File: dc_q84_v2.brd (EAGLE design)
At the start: 60.6 x 58.4 mm, 61 parts, among them IC2 7805TV, IC3 ADM3095EBRZ, IC4 PIC18F47Q84-I_PT, J1 3-1734577-4, U1 REF3440IDBVR, U2 TCAN330GDR

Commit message: up
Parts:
- removed 24VDC_PWR: 24vdc power, con-molex:22-23-2021
- removed C10, C17: 10uf, rcl:C0805
- removed C16, C9: 0.1uf, rcl:C0805
- removed U1: REF3440IDBVR, REF3440IDBVR:SOT95P280X145-6N
- removed VREF_PWR: 5vdc_vref_pwr, con-molex:22-23-2021
- moved EXT_IO 15.5 mm to (14.0, 39.4), turned to 0 degrees
- moved C3 10.9 mm to (11.4, 34.3)
- moved OS1_10MHZ 9.16 mm to (12.7, 27.9)
- moved TP2 6.84 mm to (15.2, 34.3)
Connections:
- net V+: no longer 24VDC_PWR.1
- net VDD: no longer C10.1, C9.1, U1.4
- net VREF: no longer C16.1, C17.1, U1.5, U1.6, VREF_PWR.1
- net VSS: no longer 24VDC_PWR.2, C10.2, C16.2, C17.2, C9.2, U1.1, U1.2, U1.3, VREF_PWR.2
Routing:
- net CLOCKO: track 121.4 -> 43.2 mm, vias 4 -> 0
- net PC_RX2: track 78.4 -> 25.9 mm, vias 0 -> 4
- net CANTX: track 82.4 -> 30.6 mm, vias 2 -> 4
- net V+: track 74.8 -> 26.9 mm, vias 2 -> 0
- net R_RESET: track 81.9 -> 123.6 mm, vias 5 -> 3
- net MB_TX: track 80.7 -> 48.9 mm, vias 5 -> 3
- net RE2: track 0.00 -> 31.1 mm, vias 0 -> 2
- net MISC: track 57.9 -> 29.2 mm, vias 4 -> 2
- net CANRX: track 25.5 -> 51.8 mm, vias 0 -> 2
- net CPU_CLK: track 25.7 -> 52.0 mm, vias 0 -> 1
- net MCLR_SIG: track 73.4 -> 49.5 mm, vias 8 -> 4
- net VSS: track 148.4 -> 125.4 mm, vias 8 -> 11
- net RD5: track 19.8 -> 41.1 mm, vias 0 -> 2
- net SCK1: track 85.3 -> 65.1 mm, vias 9 -> 3
- net CAN_P: track 53.9 -> 36.8 mm, vias 3 -> 0
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
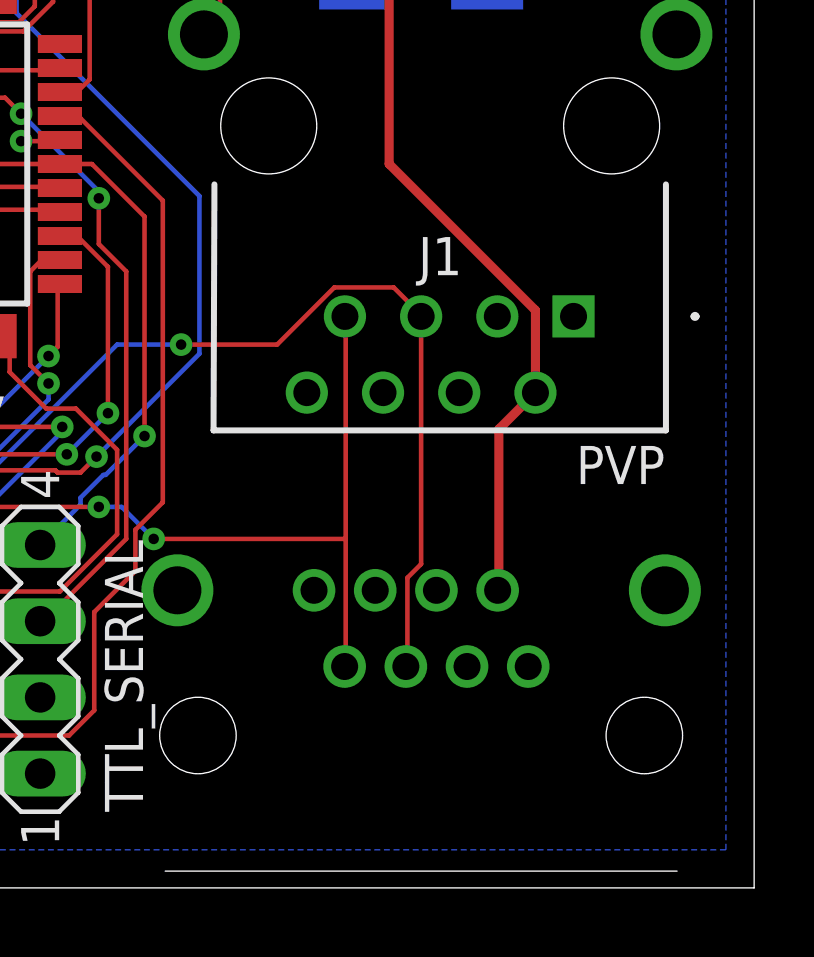
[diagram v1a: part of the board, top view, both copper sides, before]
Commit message: new rj45
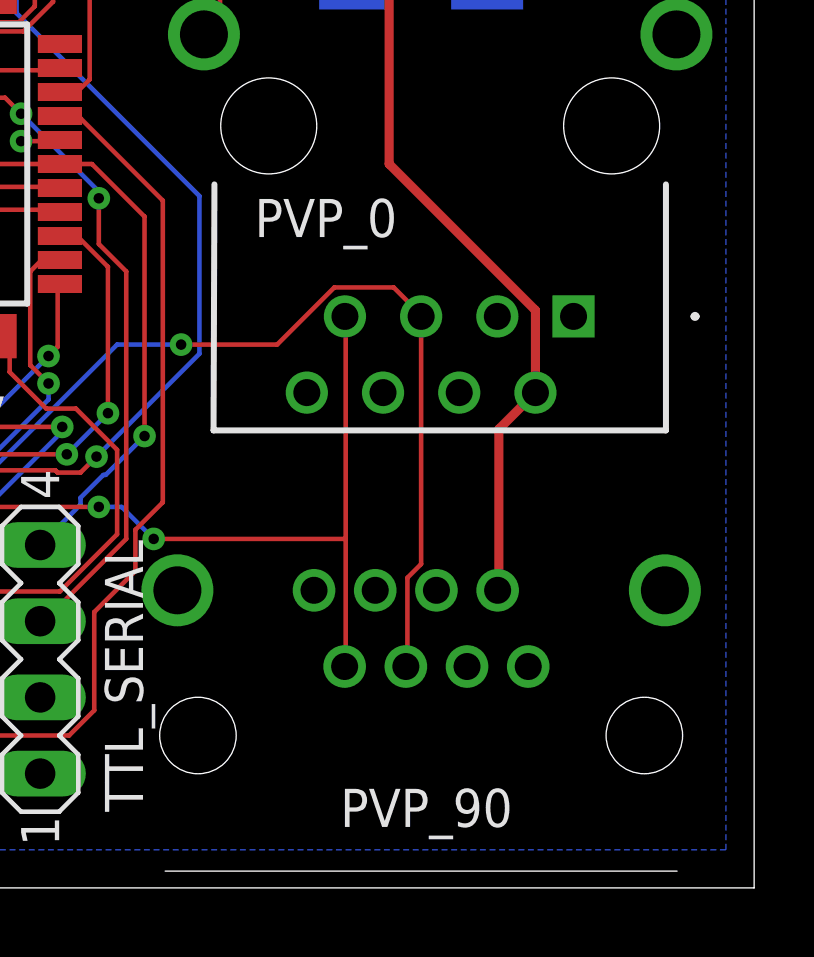
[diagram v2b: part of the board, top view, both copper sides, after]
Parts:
- renumbered J1 to PVP_0, PVP to PVP_90
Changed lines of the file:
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@@
 <attribute name="VALUE" x="0.889" y="63.5" size="1.27" layer="27" ratio="10" rot="R270"/>
 </element>
-<element name="J1" library="3-1734577-4" package="317345774" value="3-1734577-4" x="54.61" y="40.64" smashed="yes">
+<element name="PVP_0" library="3-1734577-4" package="317345774" value="3-1734577-4" x="54.61" y="40.64" smashed="yes">
 <attribute name="DESCRIPTION" value="RJ45 Connector, Single Port, 1 x 1, Standard Connector Contact Density, Jack, Shielded, Cat 3, Standard - Latch Down, 8 Position, Standard Profile " x="73.66" y="35.56" size="1.778" layer="27" display="off"/>
 <attribute name="HEIGHT" value="16.8mm" x="73.66" y="35.56" size="1.778" layer="27" display="off"/>
@@
 <attribute name="MOUSER_PART_NUMBER" value="571-3-1734577-4" x="73.66" y="35.56" size="1.778" layer="27" display="off"/>
 <attribute name="MOUSER_PRICE-STOCK" value="https://www.mouser.co.uk/ProductDetail/TE-Connectivity-AMP/3-1734577-4?qs=Z4JOKa0a9TUSCOA052xCCw%3D%3D" x="73.66" y="35.56" size="1.778" layer="27" display="off"/>
-<attribute name="NAME" x="50.165" y="42.65" size="1.27" layer="25" align="center"/>
+<attribute name="NAME" x="46.355" y="43.92" size="1.27" layer="25" align="center"/>
 <attribute name="VALUE" x="51.435" y="51.54" size="1.27" layer="27" align="center"/>
 </element>
@@
 <attribute name="VALUE" x="31.75" y="24.13" size="1.27" layer="27" rot="R90"/>
 </element>
-<element name="PVP" library="con-kycon" library_urn="urn:adsk.eagle:library:157" package="GLX-S-88M" package3d_urn="urn:adsk.eagle:package:7680/1" value="GLX-S-88M" x="49.53" y="26.67" smashed="yes" rot="R180">
+<element name="PVP_90" library="con-kycon" library_urn="urn:adsk.eagle:library:157" package="GLX-S-88M" package3d_urn="urn:adsk.eagle:package:7680/1" value="GLX-S-88M" x="49.53" y="26.67" smashed="yes" rot="R180">
 <attribute name="MF" value="" x="6.35" y="36.83" size="1.778" layer="27" rot="R180" display="off"/>
 <attribute name="MPN" value="" x="6.35" y="36.83" size="1.778" layer="27" rot="R180" display="off"/>
-<attribute name="NAME" x="57.658" y="36.322" size="1.27" layer="25" rot="R180"/>
+<attribute name="NAME" x="52.578" y="24.892" size="1.27" layer="25" rot="R180"/>
 <attribute name="OC_FARNELL" value="unknown" x="6.35" y="36.83" size="1.778" layer="27" rot="R180" display="off"/>
 <attribute name="OC_NEWARK" value="unknown" x="6.35" y="36.83" size="1.778" layer="27" rot="R180" display="off"/>
@@
 <contactref element="IC4" pad="29"/>
 <contactref element="EXT_IO" pad="1"/>
-<contactref element="PVP" pad="6"/>
-<contactref element="PVP" pad="S2"/>
-<contactref element="PVP" pad="S1"/>
+<contactref element="PVP_90" pad="6"/>
+<contactref element="PVP_90" pad="S2"/>
+<contactref element="PVP_90" pad="S1"/>
 <contactref element="DISPLAY" pad="5"/>
 <contactref element="R1" pad="2"/>
-<contactref element="J1" pad="6"/>
-<contactref element="J1" pad="10"/>
-<contactref element="J1" pad="9"/>
+<contactref element="PVP_0" pad="6"/>
+<contactref element="PVP_0" pad="10"/>
+<contactref element="PVP_0" pad="9"/>
 <polygon width="0.1524" layer="16" thermals="no" rank="6">
 <vertex x="2.54" y="78.74"/>
@@
 <signal name="V+" class="1">
 <contactref element="R12" pad="2"/>
-<contactref element="PVP" pad="2"/>
-<contactref element="J1" pad="2"/>
+<contactref element="PVP_90" pad="2"/>
+<contactref element="PVP_0" pad="2"/>
 <wire x1="48.4632" y1="45.72" x2="48.4632" y2="55.8546" width="0.3048" layer="1"/>
 <wire x1="53.34" y1="40.8432" x2="48.4632" y2="45.72" width="0.3048" layer="1"/>
@@
 <signal name="PVP_B">
 <contactref element="A+REV" pad="1"/>
-<contactref element="PVP" pad="7"/>
+<contactref element="PVP_90" pad="7"/>
 <contactref element="B-NORM" pad="1"/>
-<contactref element="J1" pad="7"/>
+<contactref element="PVP_0" pad="7"/>
 <wire x1="24.6888" y1="35.2806" x2="24.6888" y2="35.5092" width="0.1524" layer="1"/>
 <wire x1="25.7556" y1="34.2138" x2="24.6888" y2="35.2806" width="0.1524" layer="1"/>
@@
 <signal name="PVP_A">
 <contactref element="A+NORM" pad="1"/>
-<contactref element="PVP" pad="5"/>
+<contactref element="PVP_90" pad="5"/>
 <contactref element="B-REV" pad="1"/>
-<contactref element="J1" pad="5"/>
+<contactref element="PVP_0" pad="5"/>
 <wire x1="24.6888" y1="31.4706" x2="24.6888" y2="31.6992" width="0.1524" layer="1"/>
 <wire x1="25.4508" y1="30.7086" x2="24.6888" y2="31.4706" width="0.1524" layer="1"/>
